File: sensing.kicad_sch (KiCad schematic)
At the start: 22 parts, among them J3 OLED 0.91in, U10 TLV9001IDBVR, U8 INA226AIDGSR, U9 INA226AIDGSR

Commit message: fix: apply schematic review findings (VIO 5V at power-up, push-pull BOOT, input bias, CC ESD)
Co-Authored-By: Claude Opus 5.5 <noreply@anthropic.com>
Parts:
- removed U10: TLV9001IDBVR, Package_TO_SOT_SMD:SOT-23-5, symbol OOTY:TLV9001IDBV
- removed U8: INA226AIDGSR, Package_SO:MSOP-10_3x3mm_P0.5mm, symbol Sensor_Energy:INA226
- added U10: INA226AIDGSR, Package_SO:MSOP-10_3x3mm_P0.5mm, symbol Sensor_Energy:INA226
- added U11: TLV9001IDBVR, Package_TO_SOT_SMD:SOT-23-5, symbol OOTY:TLV9001IDBV
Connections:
- net +3V3: now also U10.2 (A0), U10.6 (VS), U11.5 (V+); no longer U9.2 (A0)
- net 3V3_SW: now also U10.8 (Vbus), U10.9 (Vin-); no longer U9.8 (Vbus), U9.9 (Vin-)
- net 3V3_SW_PRE: now also U10.10 (Vin+); no longer U9.10 (Vin+)
- net 5V_SW: now also U9.8 (Vbus), U9.9 (Vin-)
- net 5V_SW_PRE: now also U9.10 (Vin+)
- net AOUT_BUF: now also U11.1, U11.4 (-)
- net DAC_OUT: now also U11.3 (+)
- net GND: now also U9.2 (A0), U10.1 (A1), U10.7 (GND), U11.2 (V-)
- net I2C_INT_SCL: now also U10.5 (SCL)
- net I2C_INT_SDA: now also U10.4 (SDA)
- net INA_ALERT: now also U10.3 (~{Alert})

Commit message: fix: connect INA226 Vbus upstream of the shunt (no bias current through it)
Co-Authored-By: Claude Opus 5.5 <noreply@anthropic.com>
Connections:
- net 3V3_SW: no longer U10.8 (Vbus)
- net 3V3_SW_PRE: now also U10.8 (Vbus)
- net 5V_SW: no longer U9.8 (Vbus)
- net 5V_SW_PRE: now also U9.8 (Vbus)
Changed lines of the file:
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@@
 		)
 	)
-	(global_label "5V_SW"
+	(global_label "5V_SW_PRE"
 		(shape bidirectional)
 		(at 34.29 60.96 180)
@@
 		)
 	)
-	(global_label "3V3_SW"
+	(global_label "3V3_SW_PRE"
 		(shape bidirectional)
 		(at 35.56 140.97 180)

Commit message: fix: apply schematic review (LQFP-80 MCU, fixed-rail EN, VIO from 5V_DUT, buttons, ESD per header)
- STM32G431MBT6 (LQFP-80): 14 more GPIO; BOOT_DIR off PB4 (JTRST pull-up at reset)
- Fixed DUT rails: EN on PE7/PE8 with pull-up (on by default, firmware can cut)
- TPS2116 VIN1 from current-limited 5V_DUT instead of +5V
- Two user push buttons (TS-1187A) on PD0/PD1, BOOT0 solder jumper
- TVS after the PTC, buck Cin 10uF/25V 0805, 5th VDD decoupling cap
- No floating translator inputs (U15 A8 to GND, 1M bias on U14 B side)
- ESD channels grouped per header; datasheet field falls back to LCSC page
- Decoupling capacitors declare the pin they decouple (validated against nets)

Co-Authored-By: Claude Opus 5.5 <noreply@anthropic.com>
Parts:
- removed C31, C32: 100nF/50V, Capacitor_SMD:C_0402_1005Metric, symbol Device:C
- removed C33: 10nF/50V, Capacitor_SMD:C_0402_1005Metric, symbol Device:C
- removed R18: 50mR 1% 1W, Resistor_SMD:R_1206_3216Metric, symbol Device:R
- removed R19: 100mR 1% 1W, Resistor_SMD:R_1206_3216Metric, symbol Device:R
- removed R20, R21: 2.2k, Resistor_SMD:R_0402_1005Metric, symbol Device:R
- added C37, C38: 10nF/50V, Capacitor_SMD:C_0402_1005Metric, symbol Device:C
- added C39: 100nF/50V, Capacitor_SMD:C_0402_1005Metric, symbol Device:C
- added R30, R31, R32: 100k, Resistor_SMD:R_0402_1005Metric, symbol Device:R
- added R33: 100R, Resistor_SMD:R_0402_1005Metric, symbol Device:R
- C34, C35: value 10nF/50V -> 100nF/50V; LCSC C15195 -> C307331; MPN CL05B103KB5NNNC -> CL05B104KB54PNC
- C36: value 100nF/50V -> 10nF/50V; LCSC C307331 -> C15195; MPN CL05B104KB54PNC -> CL05B103KB5NNNC
- R22: value 10k -> 50mR 1% 1W; footprint Resistor_SMD:R_0402_1005Metric -> Resistor_SMD:R_1206_3216Metric; LCSC C25744 -> C845298; MPN 0402WGF1002TCE -> SMF12M1FR050T; Manufacturer UNI-ROYAL -> SART
- R23: value 100k -> 100mR 1% 1W; footprint Resistor_SMD:R_0402_1005Metric -> Resistor_SMD:R_1206_3216Metric; LCSC C25741 -> C201308; MPN 0402WGF1003TCE -> STE1206M1W0R100F; Manufacturer UNI-ROYAL -> Walter
- R24, R25: value 100k -> 2.2k; LCSC C25741 -> C25879; MPN 0402WGF1003TCE -> 0402WGF2201TCE
- R26: value 100k -> 10k; LCSC C25741 -> C25744; MPN 0402WGF1003TCE -> 0402WGF1002TCE
- R29: value 100R -> 100k; LCSC C25076 -> C25741; MPN 0402WGF1000TCE -> 0402WGF1003TCE
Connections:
- net +3V3: now also C34.1, C35.1, R24.2, R25.2, R26.2, C39.1; no longer C36.1, R22.2
- net 3V3_SW: now also R23.2
- net 3V3_SW_PRE: now also R23.1
- net 5V_SW: now also R22.2
- net 5V_SW_PRE: now also R22.1
- net AIN1: now also R27.1; no longer R23.1
- net AIN1_ADC: now also C36.1, R27.2, R28.1; no longer R23.2, R24.1
- net AIN2: now also R29.1; no longer R25.1
- net AIN2_ADC: now also R29.2, C37.1, R30.1; no longer C34.1, R25.2, R26.1
- net AOUT: now also R33.2; no longer R29.2
- net AOUT_BUF: now also R33.1; no longer R29.1
- net GND: now also C37.2, C38.2, C39.2, R30.2, R32.2; no longer R24.2, R26.2
- net I2C_INT_SCL: now also R25.1
- net I2C_INT_SDA: now also R24.1
- net INA_ALERT: now also R26.1; no longer R22.1
- net VIO: now also R31.1; no longer R27.1
- net VIO_MON: now also C38.1, R31.2, R32.1; no longer C35.1, R27.2, R28.1
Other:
- moved on the sheet: C34, C35, C36, R22, R23, R24, R25, R26, R27, R28, R29

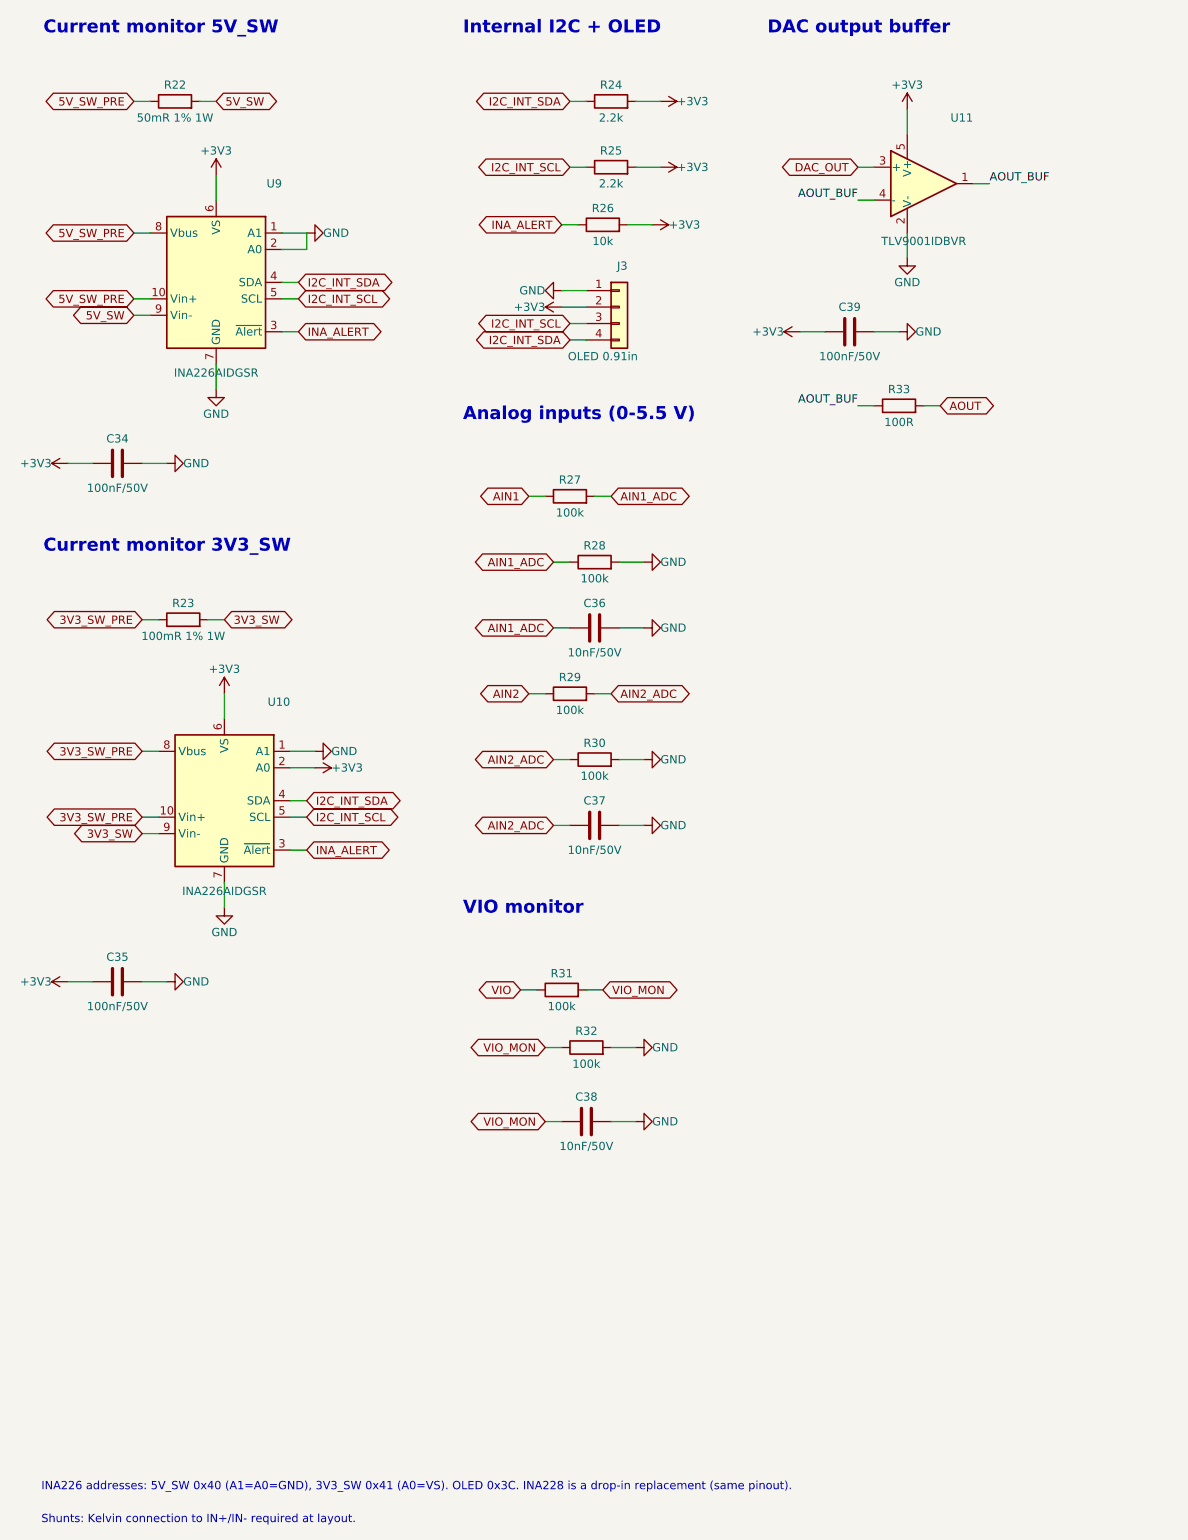
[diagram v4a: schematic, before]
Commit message: feat: dual-range current sensing and fixed-rail readback in the schematic (TASK-011)
New sheets range_5v_sw, range_3v3_sw and readback appended at the end of the
hierarchy (existing references unchanged). Shunts now end on *_MID, INA226
Vin- on *_MID, MCU pins remapped per NOTES.md. ERC 0 errors, netlist and BOM
0 mismatches.

Co-Authored-By: Claude Opus 5.5 <noreply@anthropic.com>
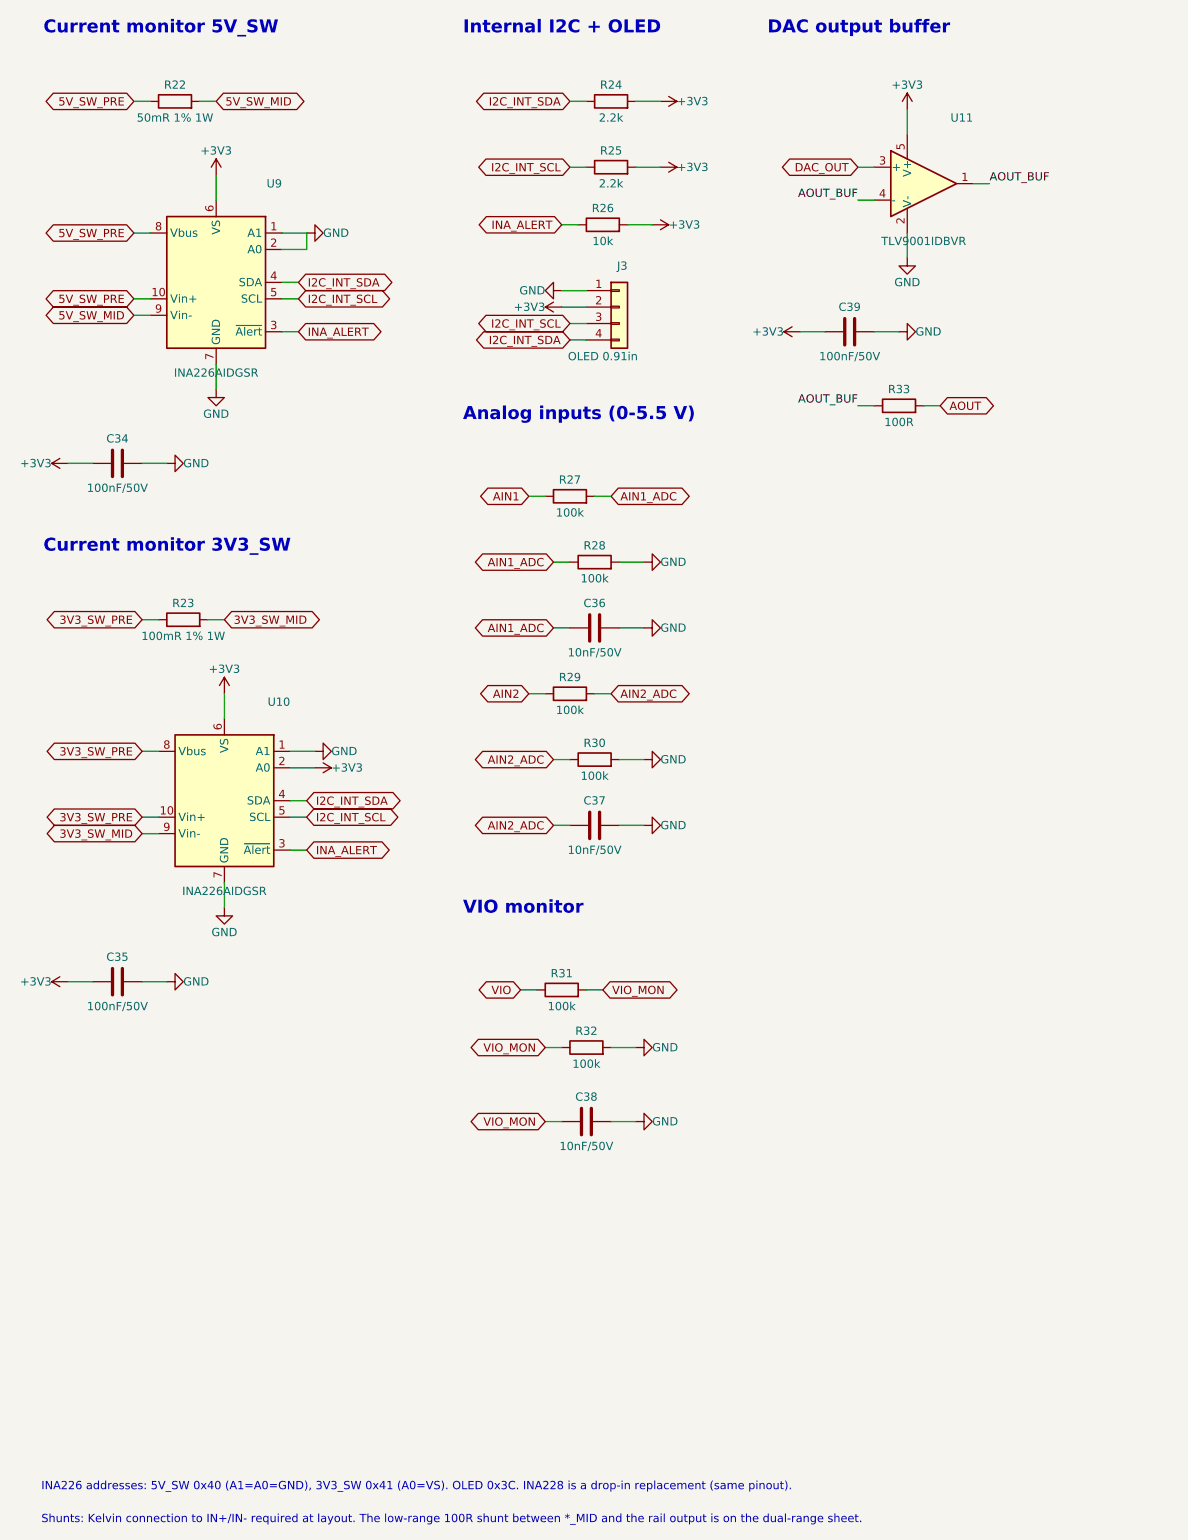
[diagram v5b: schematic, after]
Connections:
- net 3V3_SW renamed 3V3_SW_MID
- net 5V_SW renamed 5V_SW_MID
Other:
- note added: "Shunts: Kelvin connection to IN+/IN- required at layout. The low-range 100R shunt between *_MID and the rail output is on the dual-range sheet."
- note removed: "Shunts: Kelvin connection to IN+/IN- required at layout."
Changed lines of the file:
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@@
 		)
 	)
-	(text "Shunts: Kelvin connection to IN+/IN- required at layout."
+	(text "Shunts: Kelvin connection to IN+/IN- required at layout. The low-range 100R shunt between *_MID and the rail output is on the dual-range sheet."
 		(exclude_from_sim no)
 		(at 20 260.35 0)
@@
 		)
 	)
-	(global_label "3V3_SW"
+	(global_label "3V3_SW_MID"
 		(shape bidirectional)
 		(at 48.26 120.65 0)
@@
 		)
 	)
-	(global_label "5V_SW"
+	(global_label "5V_SW_MID"
 		(shape bidirectional)
 		(at 34.29 73.66 180)
@@
 		)
 	)
-	(global_label "5V_SW"
+	(global_label "5V_SW_MID"
 		(shape bidirectional)
 		(at 46.99 40.64 0)
@@
 		)
 	)
-	(global_label "3V3_SW"
+	(global_label "3V3_SW_MID"
 		(shape bidirectional)
 		(at 35.56 153.67 180)
